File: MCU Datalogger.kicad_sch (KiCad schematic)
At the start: 25 parts, among them U1 24LC1025, U2 24LC1025, U3 ATMEGA328P-AU, U4 DS1337S_, Y1 Crystal, Y2 Crystal

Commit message: assigned values
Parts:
- C1, C4: value C -> 0.1uF
- C2, C3: value C -> 22pF
- C5: value C_Polarized -> 100nF
- R1: renamed from R4; value R -> 10K
- R2: renamed from R5; value R -> 10K
- R3: renamed from R2; value R -> 4.7K
- R4: renamed from R3; value R -> 4.7K
- R5: renamed from R6; value R -> 330
- R6: renamed from R1; value R -> 10K
- R7: value R -> 330
- Y1: value Crystal -> 32.768 KHz
- Y2: value Crystal -> 16 MHz
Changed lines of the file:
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@@
 		(dnp no)
 		(fields_autoplaced yes)
-		(property "Reference" "R3"
-			(at 147.955 156.8449 0)
-			(show_name no)
-			(do_not_autoplace no)
-			(effects
-				(font
-					(size 1.27 1.27)
-				)
-				(justify left)
-			)
-		)
-		(property "Value" "R"
-			(at 147.955 159.3849 0)
+		(property "Reference" "R4"
+			(at 148.59 156.8449 0)
+			(show_name no)
+			(do_not_autoplace no)
+			(effects
+				(font
+					(size 1.27 1.27)
+				)
+				(justify left)
+			)
+		)
+		(property "Value" "4.7K"
+			(at 148.59 159.3849 0)
 			(show_name no)
 			(do_not_autoplace no)
@@
 			(at 146.05 158.115 0)
 			(hide yes)
+			(show_name no)
+			(do_not_autoplace no)
+			(effects
+				(font
+					(size 1.27 1.27)
+				)
+			)
+		)
+		(property "Purpose" ""
+			(at 146.05 158.115 0)
 			(show_name no)
 			(do_not_autoplace no)
@@
 			(project "MCU Datalogger"
 				(path "/b73ecac8-4a36-487b-b5fb-782ebc8b8ea9"
-					(reference "R3")
+					(reference "R4")
 					(unit 1)
 				)
@@
 		(dnp no)
 		(fields_autoplaced yes)
-		(property "Reference" "R2"
+		(property "Reference" "R3"
 			(at 137.16 156.8449 0)
 			(show_name no)
@@
 			)
 		)
-		(property "Value" "R"
+		(property "Value" "4.7K"
 			(at 137.16 159.3849 0)
 			(show_name no)
@@
 			(at 135.255 158.115 0)
 			(hide yes)
+			(show_name no)
+			(do_not_autoplace no)
+			(effects
+				(font
+					(size 1.27 1.27)
+				)
+			)
+		)
+		(property "Purpose" ""
+			(at 135.255 158.115 0)
 			(show_name no)
 			(do_not_autoplace no)
@@
 			(project "MCU Datalogger"
 				(path "/b73ecac8-4a36-487b-b5fb-782ebc8b8ea9"
-					(reference "R2")
+					(reference "R3")
 					(unit 1)
 				)
@@
 			)
 		)
-		(property "Value" "Crystal"
+		(property "Value" "16 MHz"
 			(at 196.85 73.025 0)
 			(show_name no)
@@
 			(at 196.85 77.47 0)
 			(hide yes)
+			(show_name no)
+			(do_not_autoplace no)
+			(effects
+				(font
+					(size 1.27 1.27)
+				)
+			)
+		)
+		(property "Purpose" ""
+			(at 196.85 77.47 0)
 			(show_name no)
 			(do_not_autoplace no)
@@
 		(dnp no)
 		(fields_autoplaced yes)
-		(property "Reference" "R4"
-			(at 93.345 54.6099 0)
-			(show_name no)
-			(do_not_autoplace no)
-			(effects
-				(font
-					(size 1.27 1.27)
-				)
-				(justify left)
-			)
-		)
-		(property "Value" "R"
-			(at 93.345 57.1499 0)
+		(property "Reference" "R1"
+			(at 93.98 54.6099 0)
+			(show_name no)
+			(do_not_autoplace no)
+			(effects
+				(font
+					(size 1.27 1.27)
+				)
+				(justify left)
+			)
+		)
+		(property "Value" "10K"
+			(at 93.98 57.1499 0)
 			(show_name no)
 			(do_not_autoplace no)
@@
 			(at 91.44 55.88 0)
 			(hide yes)
+			(show_name no)
+			(do_not_autoplace no)
+			(effects
+				(font
+					(size 1.27 1.27)
+				)
+			)
+		)
+		(property "Purpose" ""
+			(at 91.44 55.88 0)
 			(show_name no)
 			(do_not_autoplace no)
@@
 			(project "MCU Datalogger"
 				(path "/b73ecac8-4a36-487b-b5fb-782ebc8b8ea9"
-					(reference "R4")
+					(reference "R1")
 					(unit 1)
 				)
@@
 			)
 		)
-		(property "Value" "C"
+		(property "Value" "0.1uF"
 			(at 196.85 35.56 90)
 			(show_name no)
@@
 			(at 196.85 40.005 0)
 			(hide yes)
+			(show_name no)
+			(do_not_autoplace no)
+			(effects
+				(font
+					(size 1.27 1.27)
+				)
+			)
+		)
+		(property "Purpose" ""
+			(at 196.85 40.005 0)
 			(show_name no)
 			(do_not_autoplace no)
@@
 			)
 		)
-		(property "Value" "C"
+		(property "Value" "0.1uF"
 			(at 118.745 57.1499 0)
 			(show_name no)
@@
 			(at 114.935 55.88 0)
 			(hide yes)
+			(show_name no)
+			(do_not_autoplace no)
+			(effects
+				(font
+					(size 1.27 1.27)
+				)
+			)
+		)
+		(property "Purpose" ""
+			(at 114.935 55.88 0)
 			(show_name no)
 			(do_not_autoplace no)
@@
 			)
 		)
-		(property "Value" "R"
+		(property "Value" "330"
 			(at 255.905 86.3599 0)
 			(show_name no)
@@
 			(at 254 85.09 0)
 			(hide yes)
+			(show_name no)
+			(do_not_autoplace no)
+			(effects
+				(font
+					(size 1.27 1.27)
+				)
+			)
+		)
+		(property "Purpose" ""
+			(at 254 85.09 0)
 			(show_name no)
 			(do_not_autoplace no)
@@
 			)
 		)
-		(property "Value" "C_Polarized"
+		(property "Value" "100nF"
 			(at 250.825 57.15 0)
 			(show_name no)
@@
 			(at 254 51.435 0)
 			(hide yes)
+			(show_name no)
+			(do_not_autoplace no)
+			(effects
+				(font
+					(size 1.27 1.27)
+				)
+			)
+		)
+		(property "Purpose" ""
+			(at 254 51.435 0)
 			(show_name no)
 			(do_not_autoplace no)
@@
 		(dnp no)
 		(fields_autoplaced yes)
-		(property "Reference" "R6"
-			(at 180.975 50.165 90)
-			(show_name no)
-			(do_not_autoplace no)
-			(effects
-				(font
-					(size 1.27 1.27)
-				)
-			)
-		)
-		(property "Value" "R"
-			(at 180.975 52.705 90)
+		(property "Reference" "R5"
+			(at 180.975 49.53 90)
+			(show_name no)
+			(do_not_autoplace no)
+			(effects
+				(font
+					(size 1.27 1.27)
+				)
+			)
+		)
+		(property "Value" "330"
+			(at 180.975 52.07 90)
 			(show_name no)
 			(do_not_autoplace no)
@@
 			(at 180.975 55.88 0)
 			(hide yes)
+			(show_name no)
+			(do_not_autoplace no)
+			(effects
+				(font
+					(size 1.27 1.27)
+				)
+			)
+		)
+		(property "Purpose" ""
+			(at 180.975 55.88 0)
 			(show_name no)
 			(do_not_autoplace no)
@@
 			(project "MCU Datalogger"
 				(path "/b73ecac8-4a36-487b-b5fb-782ebc8b8ea9"
-					(reference "R6")
+					(reference "R5")
 					(unit 1)
 				)
@@
 		(dnp no)
 		(fields_autoplaced yes)
-		(property "Reference" "R5"
+		(property "Reference" "R2"
 			(at 105.41 54.6099 0)
 			(show_name no)
@@
 			)
 		)
-		(property "Value" "R"
+		(property "Value" "10K"
 			(at 105.41 57.1499 0)
 			(show_name no)
@@
 			(at 103.505 55.88 0)
 			(hide yes)
+			(show_name no)
+			(do_not_autoplace no)
+			(effects
+				(font
+					(size 1.27 1.27)
+				)
+			)
+		)
+		(property "Purpose" ""
+			(at 103.505 55.88 0)
 			(show_name no)
 			(do_not_autoplace no)
@@
 			(project "MCU Datalogger"
 				(path "/b73ecac8-4a36-487b-b5fb-782ebc8b8ea9"
-					(reference "R5")
+					(reference "R2")
 					(unit 1)
 				)
@@
 		(dnp no)
 		(fields_autoplaced yes)
-		(property "Reference" "R1"
+		(property "Reference" "R6"
 			(at 196.85 85.09 90)
 			(show_name no)
@@
 			)
 		)
-		(property "Value" "R"
+		(property "Value" "10K"
 			(at 196.85 87.63 90)
 			(show_name no)
@@
 			(at 196.85 91.44 0)
 			(hide yes)
+			(show_name no)
+			(do_not_autoplace no)
+			(effects
+				(font
+					(size 1.27 1.27)
+				)
+			)
+		)
+		(property "Purpose" ""
+			(at 196.85 91.44 0)
 			(show_name no)
 			(do_not_autoplace no)
@@
 			(project "MCU Datalogger"
 				(path "/b73ecac8-4a36-487b-b5fb-782ebc8b8ea9"
-					(reference "R1")
+					(reference "R6")
 					(unit 1)
 				)
@@
 			)
 		)
-		(property "Value" "C"
+		(property "Value" "22pF"
 			(at 184.785 72.3899 0)
 			(show_name no)
@@
 			(at 180.975 71.12 0)
 			(hide yes)
+			(show_name no)
+			(do_not_autoplace no)
+			(effects
+				(font
+					(size 1.27 1.27)
+				)
+			)
+		)
+		(property "Purpose" ""
+			(at 180.975 71.12 0)
 			(show_name no)
 			(do_not_autoplace no)
@@
 			)
 		)
-		(property "Value" "C"
+		(property "Value" "22pF"
 			(at 184.785 87.6299 0)
 			(show_name no)
@@
 			(at 180.975 86.36 0)
 			(hide yes)
+			(show_name no)
+			(do_not_autoplace no)
+			(effects
+				(font
+					(size 1.27 1.27)
+				)
+			)
+		)
+		(property "Purpose" ""
+			(at 180.975 86.36 0)
 			(show_name no)
 			(do_not_autoplace no)
@@
 			)
 		)
-		(property "Value" "Crystal"
+		(property "Value" "32.768 KHz"
 			(at 31.75 59.69 0)
 			(show_name no)
@@
 			(show_name no)
 			(do_not_autoplace no)
+			(effects
+				(font
+					(size 1.27 1.27)
+				)
+			)
+		)
+		(property "Purpose" ""
+			(at 31.75 64.135 0)
+			(show_name no)
+			(do_not_autoplace no)

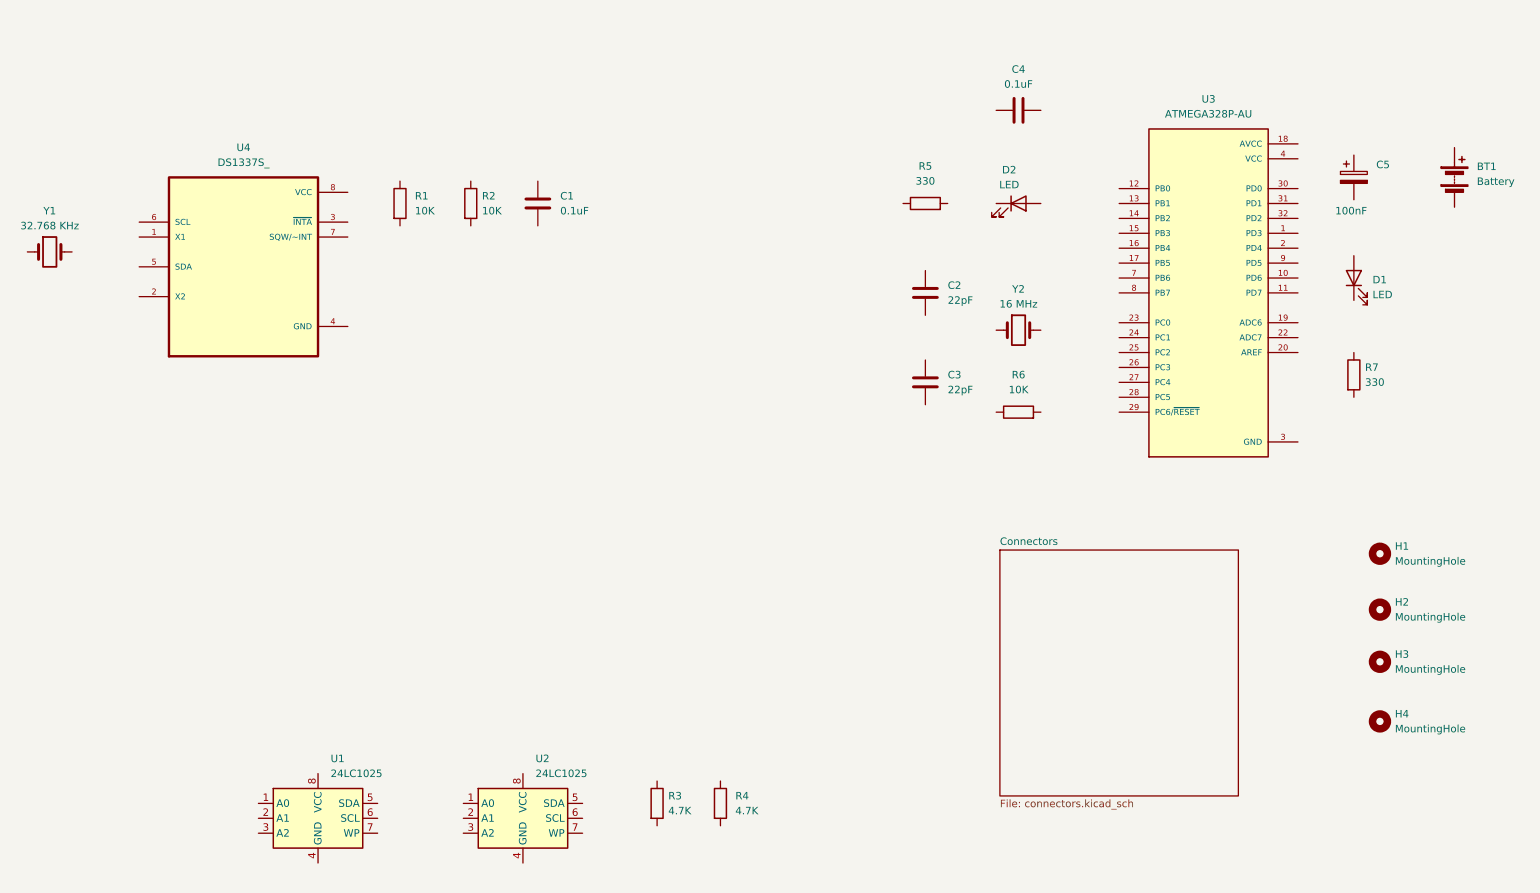
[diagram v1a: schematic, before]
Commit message: assigned footprints
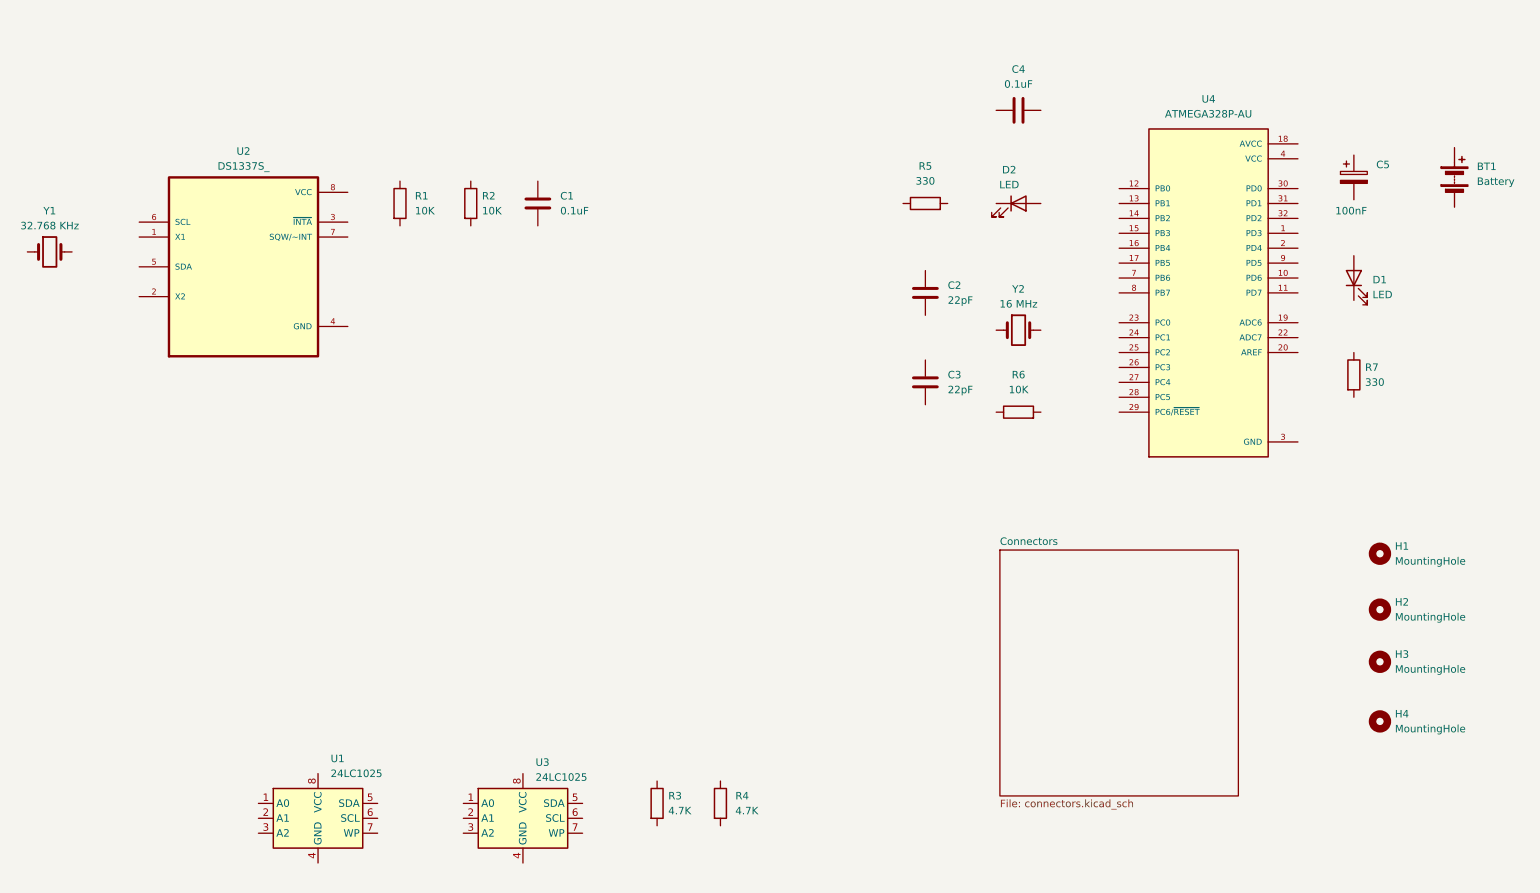
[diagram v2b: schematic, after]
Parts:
- BT1: footprint (none) -> Connector_PinHeader_2.54mm:PinHeader_1x02_P2.54mm_Vertical
- C1, C2, C3, C4, C5: footprint (none) -> Capacitor_SMD:C_0805_2012Metric
- D1, D2: footprint (none) -> LED_SMD:LED_0805_2012Metric
- H1, H2, H3, H4: footprint (none) -> MountingHole:MountingHole_2.1mm
- R1, R2, R3, R4, R5, R6, R7: footprint (none) -> Resistor_SMD:R_0805_2012Metric
- U1: footprint (none) -> Package_SO:SOIC-8_5.3x5.3mm_P1.27mm
- U3: renamed from U2; footprint (none) -> Package_SO:SOIC-8_5.3x5.3mm_P1.27mm
- Y1, Y2: footprint (none) -> Crystal:Crystal_SMD_5032-2Pin_5.0x3.2mm_HandSoldering
- renumbered U4 to U2, U3 to U4
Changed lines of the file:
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@@
 			)
 		)
-		(property "Footprint" ""
+		(property "Footprint" "MountingHole:MountingHole_2.1mm"
 			(at 258.445 125.095 0)
 			(hide yes)
@@
 			)
 		)
-		(property "Footprint" ""
+		(property "Footprint" "Resistor_SMD:R_0805_2012Metric"
 			(at 144.272 158.115 90)
 			(hide yes)
@@
 			)
 		)
-		(property "Footprint" ""
+		(property "Footprint" "Resistor_SMD:R_0805_2012Metric"
 			(at 133.477 158.115 90)
 			(hide yes)
@@
 			)
 		)
-		(property "Footprint" ""
+		(property "Footprint" "Crystal:Crystal_SMD_5032-2Pin_5.0x3.2mm_HandSoldering"
 			(at 196.85 77.47 0)
 			(hide yes)
@@
 			)
 		)
-		(property "Footprint" ""
+		(property "Footprint" "Resistor_SMD:R_0805_2012Metric"
 			(at 89.662 55.88 90)
 			(hide yes)
@@
 			)
 		)
-		(property "Footprint" ""
+		(property "Footprint" "Connector_PinHeader_2.54mm:PinHeader_1x02_P2.54mm_Vertical"
 			(at 271.145 49.911 90)
 			(hide yes)
@@
 			)
 		)
-		(property "Footprint" ""
+		(property "Footprint" "Capacitor_SMD:C_0805_2012Metric"
 			(at 200.66 39.0398 0)
 			(hide yes)
@@
 			)
 		)
-		(property "Footprint" ""
+		(property "Footprint" "Package_SO:SOIC-8_5.3x5.3mm_P1.27mm"
 			(at 77.47 160.655 0)
 			(hide yes)
@@
 			)
 		)
-		(property "Footprint" ""
+		(property "Footprint" "Capacitor_SMD:C_0805_2012Metric"
 			(at 115.9002 59.69 0)
 			(hide yes)
@@
 			)
 		)
-		(property "Footprint" ""
+		(property "Footprint" "LED_SMD:LED_0805_2012Metric"
 			(at 254 68.58 0)
 			(hide yes)
@@
 		(dnp no)
 		(fields_autoplaced yes)
-		(property "Reference" "U3"
+		(property "Reference" "U4"
 			(at 229.235 38.1 0)
 			(show_name no)
@@
 			(project "MCU Datalogger"
 				(path "/b73ecac8-4a36-487b-b5fb-782ebc8b8ea9"
-					(reference "U3")
+					(reference "U4")
 					(unit 1)
 				)
@@
 			)
 		)
-		(property "Footprint" ""
+		(property "Footprint" "Resistor_SMD:R_0805_2012Metric"
 			(at 252.222 85.09 90)
 			(hide yes)
@@
 			)
 		)
-		(property "Footprint" ""
+		(property "Footprint" "Capacitor_SMD:C_0805_2012Metric"
 			(at 254.9652 55.245 0)
 			(hide yes)
@@
 			)
 		)
-		(property "Footprint" ""
+		(property "Footprint" "LED_SMD:LED_0805_2012Metric"
 			(at 196.85 55.88 0)
 			(hide yes)
@@
 		(dnp no)
 		(fields_autoplaced yes)
-		(property "Reference" "U2"
-			(at 114.5383 150.495 0)
+		(property "Reference" "U3"
+			(at 114.5383 151.13 0)
 			(show_name no)
 			(do_not_autoplace no)
@@
 		)
 		(property "Value" "24LC1025"
-			(at 114.5383 153.035 0)
-			(show_name no)
-			(do_not_autoplace no)
-			(effects
-				(font
-					(size 1.27 1.27)
-				)
-				(justify left)
-			)
-		)
-		(property "Footprint" ""
+			(at 114.5383 153.67 0)
+			(show_name no)
+			(do_not_autoplace no)
+			(effects
+				(font
+					(size 1.27 1.27)
+				)
+				(justify left)
+			)
+		)
+		(property "Footprint" "Package_SO:SOIC-8_5.3x5.3mm_P1.27mm"
 			(at 112.395 160.655 0)
 			(hide yes)
@@
 			(project "MCU Datalogger"
 				(path "/b73ecac8-4a36-487b-b5fb-782ebc8b8ea9"
-					(reference "U2")
+					(reference "U3")
 					(unit 1)
 				)
@@
 			)
 		)
-		(property "Footprint" ""
+		(property "Footprint" "Resistor_SMD:R_0805_2012Metric"
 			(at 180.975 57.658 90)
 			(hide yes)
@@
 			)
 		)
-		(property "Footprint" ""
+		(property "Footprint" "MountingHole:MountingHole_2.1mm"
 			(at 258.445 133.985 0)
 			(hide yes)
@@
 			)
 		)
-		(property "Footprint" ""
+		(property "Footprint" "Resistor_SMD:R_0805_2012Metric"
 			(at 101.727 55.88 90)
 			(hide yes)
@@
 			)
 		)
-		(property "Footprint" ""
+		(property "Footprint" "Resistor_SMD:R_0805_2012Metric"
 			(at 196.85 93.218 90)
 			(hide yes)
@@
 			)
 		)
-		(property "Footprint" ""
+		(property "Footprint" "Capacitor_SMD:C_0805_2012Metric"
 			(at 181.9402 74.93 0)
 			(hide yes)
@@
 			)
 		)
-		(property "Footprint" ""
+		(property "Footprint" "Capacitor_SMD:C_0805_2012Metric"
 			(at 181.9402 90.17 0)
 			(hide yes)
@@
 			)
 		)
-		(property "Footprint" ""
+		(property "Footprint" "MountingHole:MountingHole_2.1mm"
 			(at 258.445 115.57 0)
 			(hide yes)
@@
 			)
 		)
-		(property "Footprint" ""
+		(property "Footprint" "MountingHole:MountingHole_2.1mm"
 			(at 258.445 144.145 0)
 			(hide yes)
@@
 			)
 		)
-		(property "Footprint" ""
+		(property "Footprint" "Crystal:Crystal_SMD_5032-2Pin_5.0x3.2mm_HandSoldering"
 			(at 31.75 64.135 0)
 			(hide yes)
@@
 		(dnp no)
 		(fields_autoplaced yes)
-		(property "Reference" "U4"
-			(at 64.77 46.355 0)
+		(property "Reference" "U2"
+			(at 64.77 46.99 0)
 			(show_name no)
 			(do_not_autoplace no)
@@
 		)
 		(property "Value" "DS1337S_"
-			(at 64.77 48.895 0)
+			(at 64.77 49.53 0)
 			(show_name no)
 			(do_not_autoplace no)
@@
 			(project "MCU Datalogger"
 				(path "/b73ecac8-4a36-487b-b5fb-782ebc8b8ea9"
-					(reference "U4")
+					(reference "U2")
 					(unit 1)
 				)
